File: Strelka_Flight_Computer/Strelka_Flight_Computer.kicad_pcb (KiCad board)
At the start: 4 copper layers, 91 x 30.1 mm, 168 parts, among them IC1 XTSD04GLGEAG, IC2 MAX-M10S-00B, J2 Conn_01x04, J3 DB125-3.5-4P-GN-S, J4 SM06B-GHS-TB(LF)(SN), J6 USB_B_Micro, J7 Conn_01x02, J8 Conn_01x07, Q1 CJK2333, Q10 AP2300, Q11 MMBT2222, Q15 AO3400A, Q16 AO3400A, Q17 AO3401A, Q2 CJK2333, Q4 AO3401A, Q5 AP2300, Q6 MMBT2222, Q9 AO3401A, SW1 SW_DIP_x01, SW6 TS-1185-C-A-A-A, SW7 TS-1185-C-A-A-A, U1 ASM330LHHXTR, U11 BMX055, U12 MS561101BA03-50, U16 TPS61085DGKR, U2 AP9101CK6, U3 AMS1117-3.3, U4 RFM95W-915S2, U5 MCP2551-I-SN, U6 STM32H743VITx, U8 USBLC6-2SC6, Y5 Q13FC1350000400, Y6 X1E0000210834

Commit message: Routing complete
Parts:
- removed C36: 100n, Capacitor_SMD:C_0402_1005Metric
- removed JP6, JP7: Jumper_2_Bridged, Jumper:SolderJumper-2_P1.3mm_Bridged2Bar_RoundedPad1.0x1.5mm
- added G***: LOGO, Footprints:Strelka_Logo, F.Cu at (159.9, 36.0)
- BT2, D11, MOSFET1, Q16, Q17, R1, U2: moved to B.Cu
- D12: value LED_BLUE -> LED_GREEN
- D18: value BLUE LED -> RED LED
- D20: value RED LED -> BLUE LED
- moved D19 147.4 mm to (107.9, 67.8)
- moved D20 143.8 mm to (119.1, 55.5), turned to 90 degrees
- moved R77 136.9 mm to (105.4, 67.5)
- moved R78 134.9 mm to (115.4, 54.2)
- moved C40 130.1 mm to (188.2, 57.3)
- moved C39 126.6 mm to (185.7, 57.3), turned to 180 degrees
- moved C11 125.9 mm to (174.7, 75.0), turned to 180 degrees
- moved C10 123.7 mm to (174.7, 76.5), turned to 180 degrees
- moved Q17 121.8 mm to (138.4, 55.2)
- moved C60 120.1 mm to (147.0, 63.2), turned to 135 degrees
- moved C1 119.6 mm to (145.0, 64.9), turned to -90 degrees
- moved C29 117.3 mm to (179.1, 67.8), turned to -90 degrees
- moved C54 117.0 mm to (158.8, 52.6), turned to 135 degrees
- moved C52 116.4 mm to (147.7, 62.5), turned to 135 degrees
- moved C28 115.9 mm to (180.5, 68.2)
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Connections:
- net /Actuators/Ematch_Drogue1/EMATCH+ renamed /Actuators/D+
- net /Actuators/Ematch_Drogue1/EMATCH- renamed /Actuators/D-
- net /Actuators/Ematch_Main/EMATCH+ renamed /Actuators/M+
- net /Actuators/Ematch_Main/EMATCH- renamed /Actuators/M-
- net Net-(Q4-S) renamed /Actuators/Ematch_Drogue1/em+
- net Net-(Q9-S) renamed /Actuators/Ematch_Main/em+
- C10 pad 1: +3V3 -> +3.3V
- C11 pad 1: +3V3 -> +3.3V
- C39 pad 1: +3V3 -> +3.3V
- C40 pad 1: +3V3 -> +3.3V
- C7 pad 1: +3V3 -> +3.3V
- C8 pad 1: +3V3 -> +3.3V
- D11 pad 1: +3V3 -> +3.3V
- IC2 pad 7: +3V3 -> +3.3V
- IC2 pad 8: +3V3 -> +3.3V
- R1 pad 1: unconnected-(R1-Pad1) -> -BATT
- R77 pad 1: Net-(JP6-B) -> GND
- R78 pad 1: Net-(JP7-B) -> GND
- TP4 pad 1: +3V3 -> +3.3V
- U3 pad 2: +3V3 -> +3.3V
- U4 pad 13: +3V3 -> +3.3V
- U6 pad 90: unconnected-(U6-PB4-Pad90) -> /Actuators/DROGUE_H
- U6 pad 91: unconnected-(U6-PB5-Pad91) -> /Actuators/DROGUE_L
- U6 pad 92: unconnected-(U6-PB6-Pad92) -> /Actuators/MAIN_H
- U6 pad 93: unconnected-(U6-PB7-Pad93) -> /Actuators/MAIN_L
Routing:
- net +3.3V: track 27.2 -> 71.6 mm, vias 10 -> 33
- net VDC: track 0.00 -> 41.1 mm, vias 0 -> 4
- net /STM32H743/NRST: track 0.00 -> 38.7 mm, vias 0 -> 2
- net /STM32H743/SWO: track 0.00 -> 38.3 mm, vias 0 -> 4
- net /STM32H743/SWCLK: track 0.00 -> 37.3 mm, vias 0 -> 4
- net /STM32H743/SWDIO: track 0.00 -> 36.8 mm, vias 0 -> 4
- net +5V: track 48.3 -> 84.3 mm, vias 2 -> 5
- net GND: track 7.97 -> 42.4 mm, vias 12 -> 47
- net /Sensors/MAX-M10S-00B/V_BKCP: track 0.00 -> 34.1 mm, vias 0 -> 2
- net /Actuators/M+: track 0.00 -> 28.3 mm, vias 0 -> 1
- net /Actuators/DROGUE_L: track 0.00 -> 26.9 mm, vias 0 -> 3
- net /STM32H743/BOOT0: track 0.00 -> 26.1 mm, vias 0 -> 2
- net /Actuators/D+: track 0.00 -> 25.9 mm, vias 0 -> 1
- net /Actuators/DROGUE_H: track 0.00 -> 22.2 mm, vias 0 -> 2
- net /Actuators/MAIN_H: track 0.00 -> 18.1 mm, vias 0 -> 2
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- added copper zone on F.Cu, net +3.3V
- added copper zone on In2.Cu, net +3.3V
- added copper zone on B.Cu, net GND
- added copper zone on F.Cu, net GND
- added copper zone on In1.Cu, net GND
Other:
- board text added: "DROGUE"
- board text added: "Flight Computer"
- board text added: "GPS PPS"
- board text added: "MAIN"
- board text added: "Strelka v2"

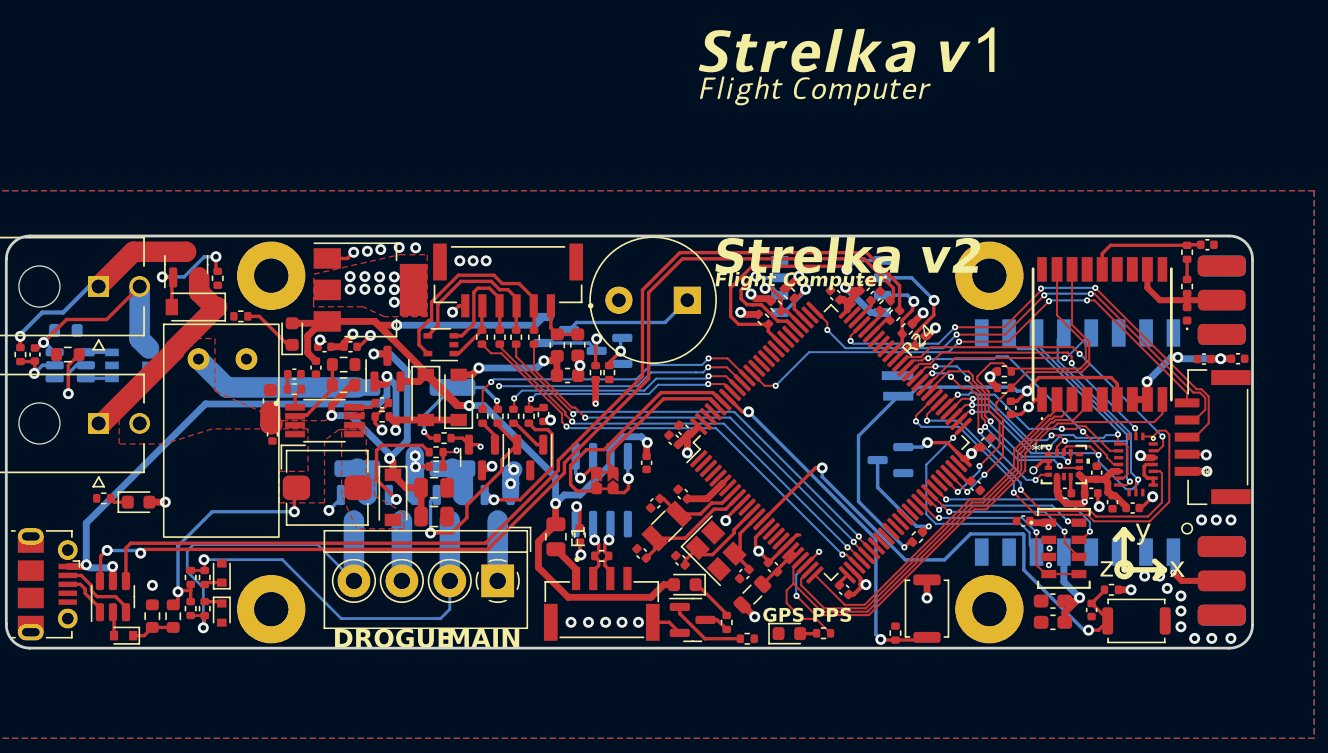
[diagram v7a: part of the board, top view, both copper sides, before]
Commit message: Created BOM
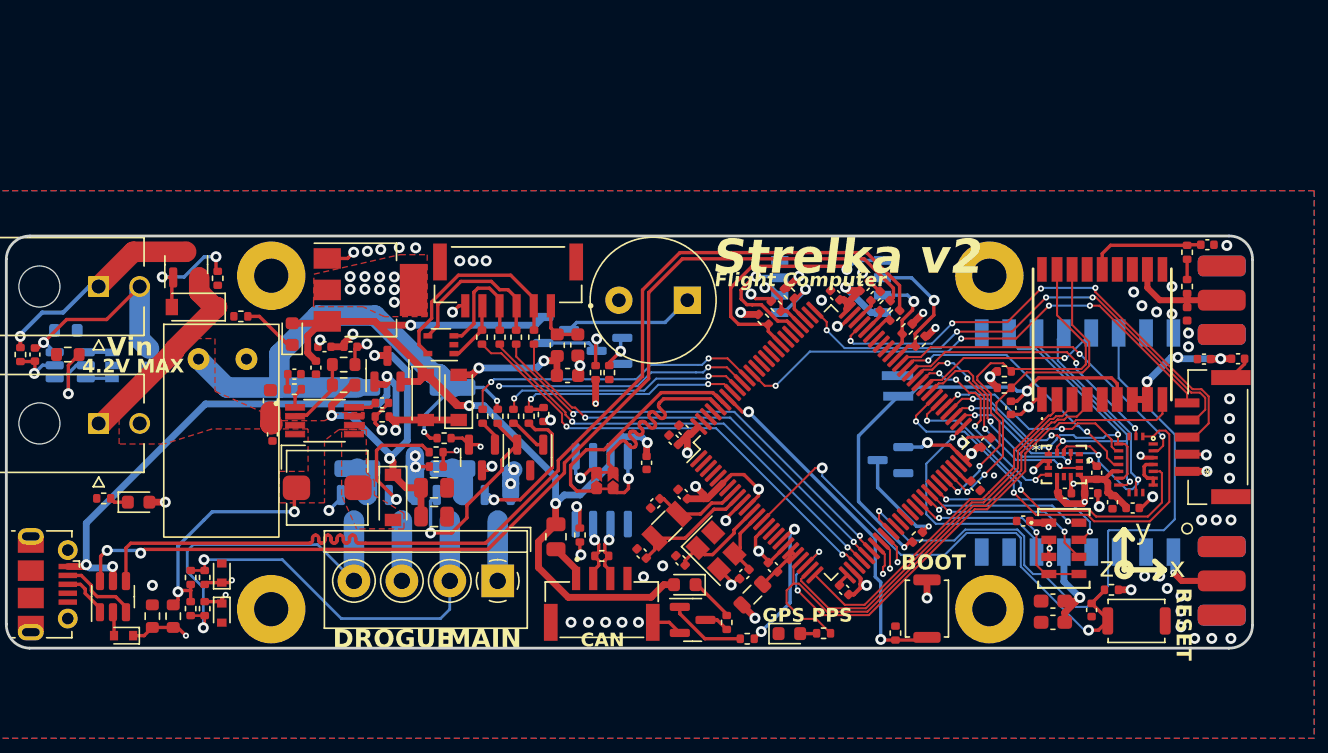
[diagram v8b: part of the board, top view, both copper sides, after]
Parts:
- removed G***: LOGO, Footprints:Strelka_Logo
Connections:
- U6 pad 18: unconnected-(U6-PC3_C-Pad18) -> /STM32H743/INDICATOR_LED
- U6 pad 32: unconnected-(U6-PC4-Pad32) -> /Power/BATT_VOLT
- U6 pad 33: unconnected-(U6-PC5-Pad33) -> /Actuators/DROGUE_CONT
- U6 pad 34: unconnected-(U6-PB0-Pad34) -> /Actuators/MAIN_CONT
- U6 pad 35: unconnected-(U6-PB1-Pad35) -> /915MHz_Radio/RESET_RF
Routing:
- net /Power/BATT_VOLT: track 3.17 -> 64.0 mm, vias 0 -> 2
- net /Actuators/DROGUE_CONT: track 1.31 -> 58.3 mm, vias 0 -> 2
- net /Actuators/MAIN_CONT: track 1.31 -> 57.7 mm, vias 0 -> 2
- net /915MHz_Radio/RESET_RF: track 0.00 -> 48.5 mm, vias 0 -> 1
- net VDC: track 41.1 -> 59.5 mm
- net GND: track 42.4 -> 54.3 mm, vias 47 -> 70
- net /STM32H743/INDICATOR_LED: track 0.00 -> 10.6 mm, vias 0 -> 2
- net /Data_Interfaces/CAN_P: track 11.3 -> 16.8 mm
- net +3.3V: track 71.6 -> 77.1 mm, vias 33 -> 35
- net /Data_Interfaces/USB_D-: track 74.8 -> 77.8 mm
- net +5V: track 84.3 -> 82.5 mm
- net /STM32H743/NRST: track 38.7 -> 38.1 mm
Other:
- board text added: "4.2V MAX"
- board text added: "BOOT"
- board text added: "CAN"
- board text added: "RESET"
- board text added: "Vin"
